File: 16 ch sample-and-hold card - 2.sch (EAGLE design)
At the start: 80 parts, among them IC1 TL074D, IC3 TL074D, IC4 TL074D, IC7 TL074D, IC9 MAX306CWI

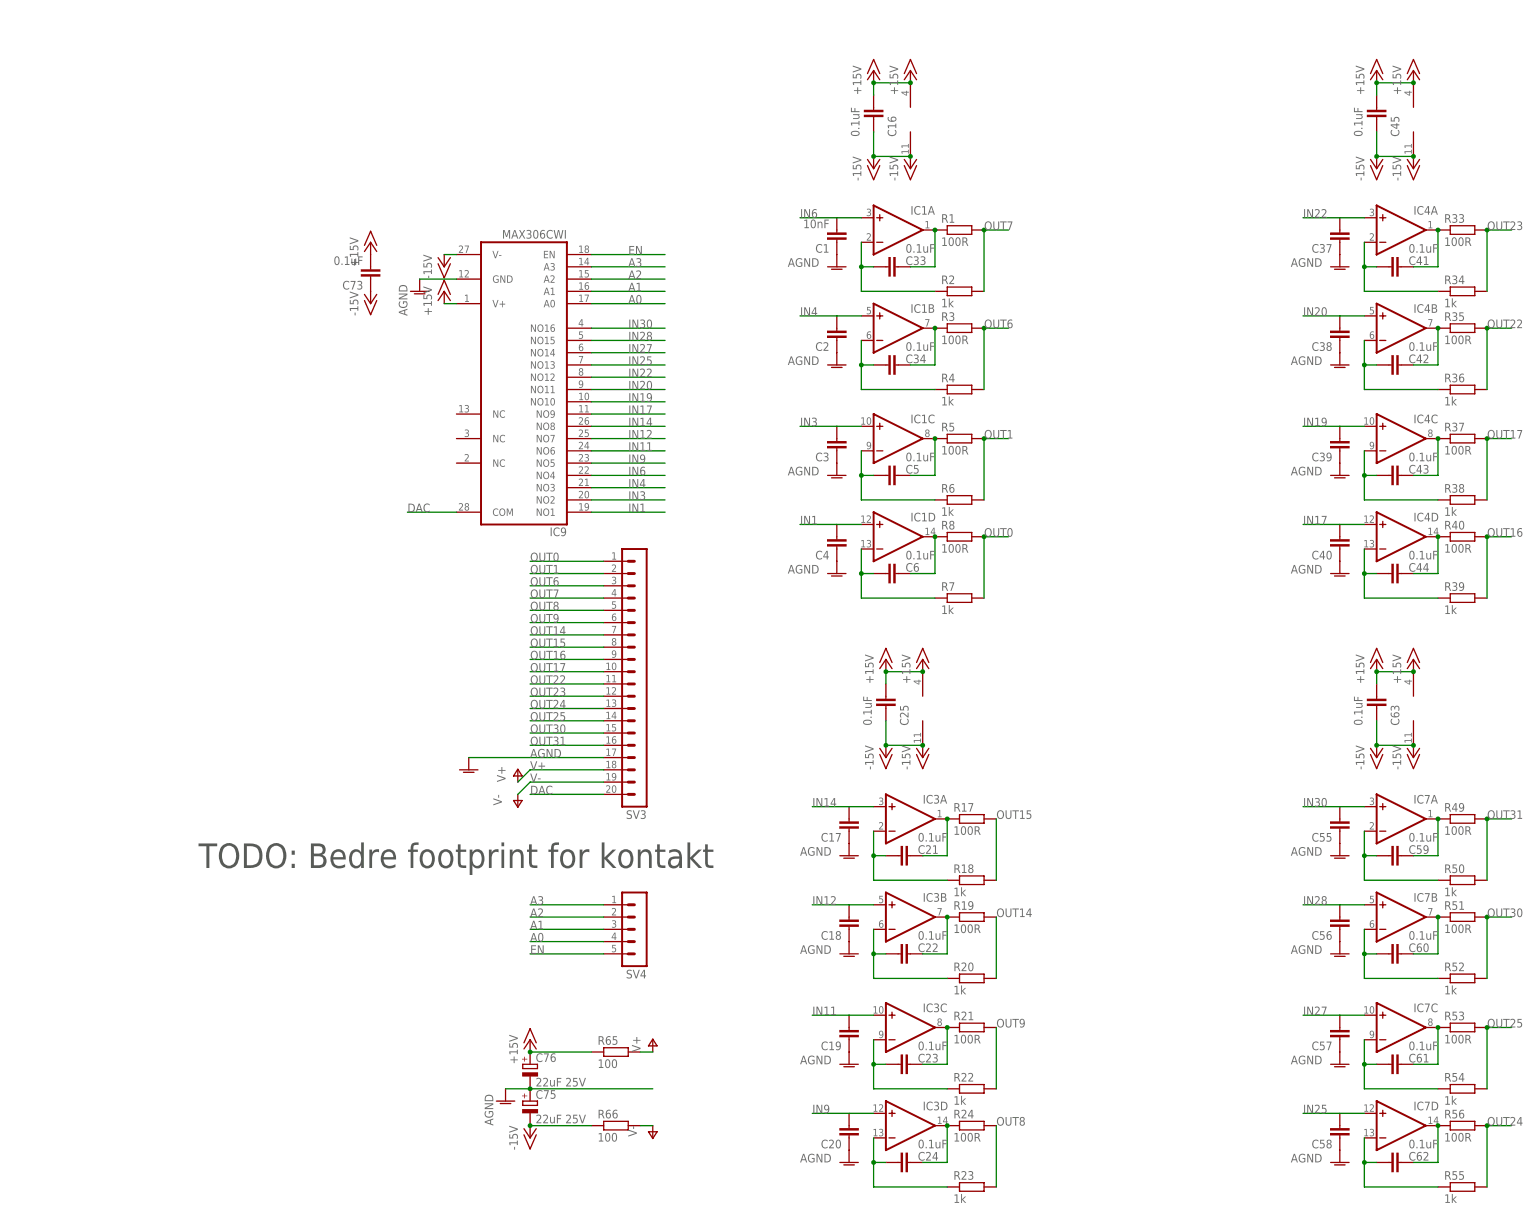
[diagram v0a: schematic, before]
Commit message: Reworked resistor and electrolytic caps placement to tap power AFTER caps for better noise filtering
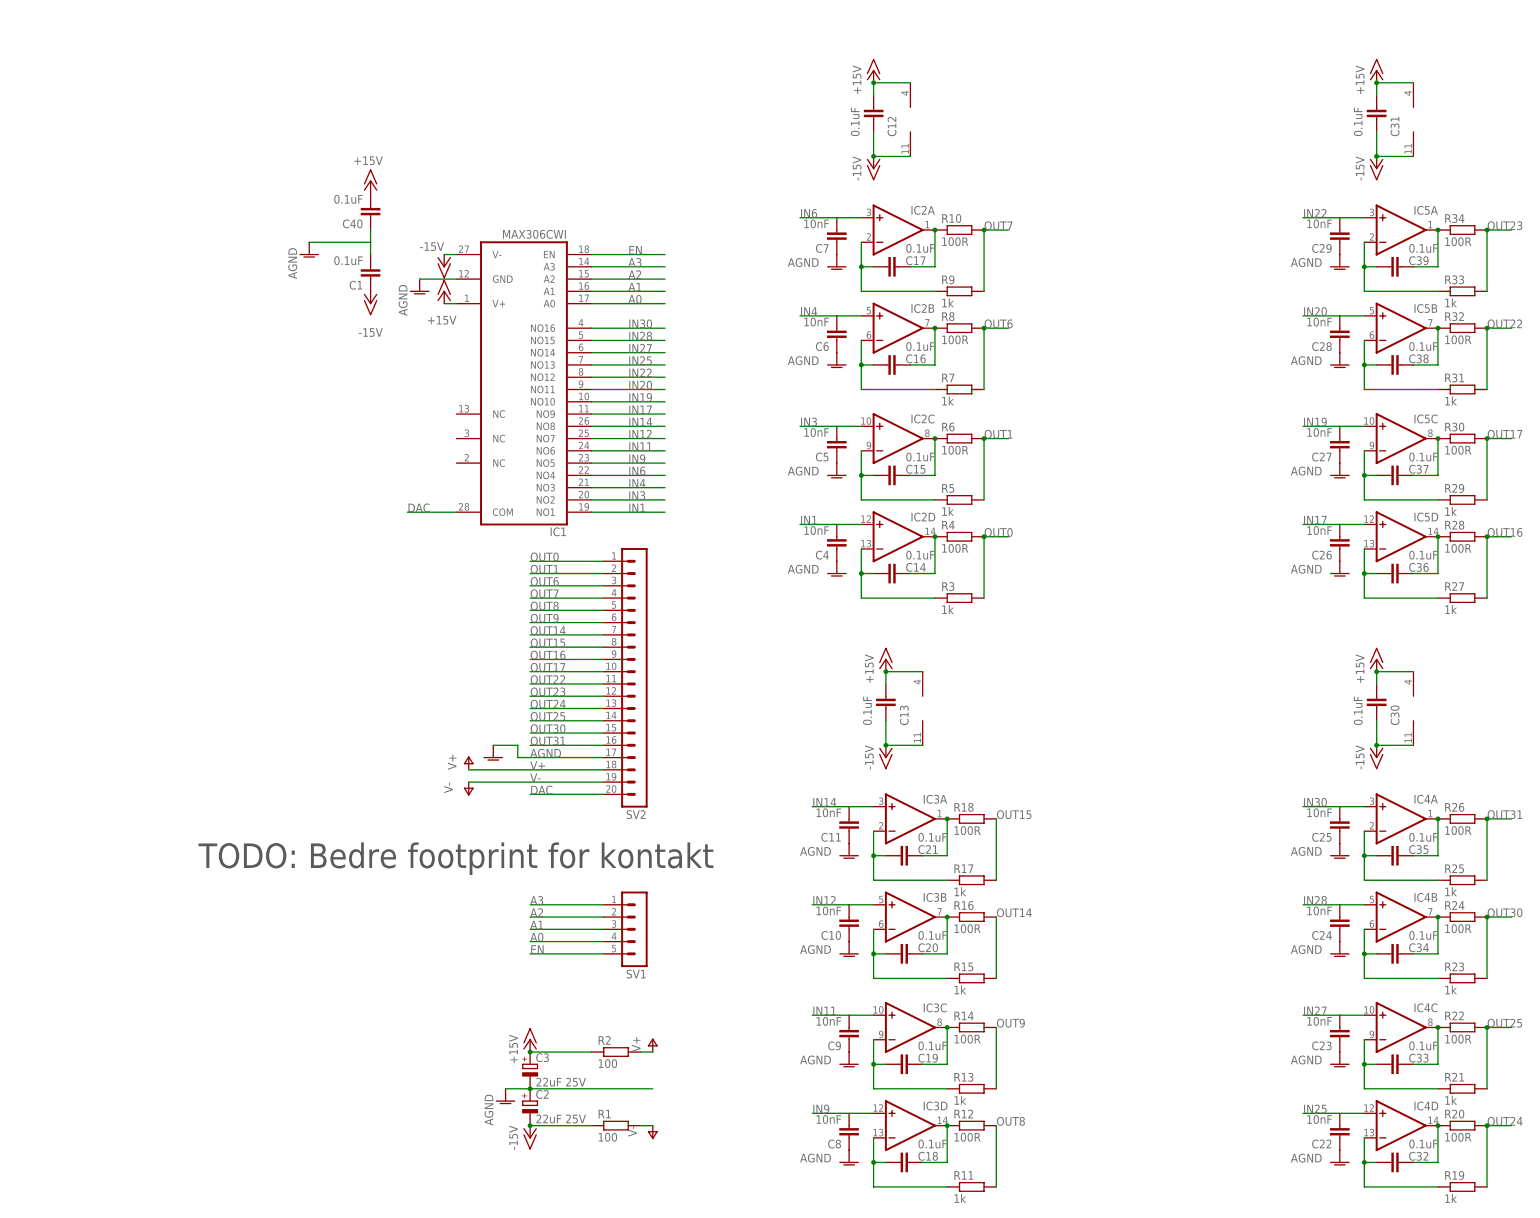
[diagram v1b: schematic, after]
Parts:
- removed C41, C42, C43, C60, C61, C73: 0.1uF, resistor:C-EUC0603
- removed C55, C56, C57, C58: (no value), resistor:C-EUC1206
- removed C75, C76: 22uF 25V, resistor:CPOL-EUE2-5
- removed IC7: TL074D, linear:TL074D
- removed IC9: MAX306CWI, maxim:MAX306CWI
- removed R51, R53, R56: 100R, resistor:R-EU_R0603
- removed R52, R54, R55: 1k, resistor:R-EU_R0603
- removed R65, R66: 100, resistor:R-EU_0207/7
- added C10, C11, C26, C27, C28, C29, C7, C8, C9: 10nF, resistor:C-EUC1206
- added C12, C13, C14, C15: 0.1uF, resistor:C-EUC0603
- added IC2, IC5: TL074D, linear:TL074D
- added R10, R12, R14, R16: 100R, resistor:R-EU_R0603
- added R11, R13, R15, R9: 1k, resistor:R-EU_R0603
- C1: value 10nF -> 0.1uF; device resistor:C-EUC1206 -> resistor:C-EUC0603
- C17, C18, C19, C20, C37, C38, C39, C40: value (none) -> 0.1uF; device resistor:C-EUC1206 -> resistor:C-EUC0603
- C2, C3: value (none) -> 22uF 25V; device resistor:C-EUC1206 -> resistor:CPOL-EUE2-5
- C22, C23, C24, C25, C5, C6: value 0.1uF -> 10nF; device resistor:C-EUC0603 -> resistor:C-EUC1206
- C4: value (none) -> 10nF
- IC1: value TL074D -> MAX306CWI; device linear:TL074D -> maxim:MAX306CWI
- R1: value 100R -> 100; device resistor:R-EU_R0603 -> resistor:R-EU_0207/7
- R17, R19, R21, R3, R33, R5: value 100R -> 1k
- R18, R20, R22, R34, R4, R6: value 1k -> 100R
- R2: value 1k -> 100; device resistor:R-EU_R0603 -> resistor:R-EU_0207/7
- renumbered C44 to C36, C45 to C31, C59 to C35, C62 to C32, C63 to C30, R35 to R32, R36 to R31, R37 to R30, R38 to R29, R39 to R27, R40 to R28, R49 to R26, R50 to R25, SV3 to SV2, SV4 to SV1
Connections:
- net +15V: now also C12.1, C13.1, C3.+, C40.2, IC1.V+, IC2P.V+, IC5P.V+, R2.1; no longer C16.1, C25.1, C73.2, C76.+, IC1P.V+, IC7P.V+, IC9.V+, R65.1
- net -15V: now also C1.1, C12.2, C13.2, C2.-, IC1.V-, IC2P.V-, IC5P.V-, R1.1; no longer C16.2, C25.2, C73.1, C75.-, IC1P.V-, IC7P.V-, IC9.V-, R66.1
- net A0: now also IC1.A0; no longer IC9.A0
- net A1: now also IC1.A1; no longer IC9.A1
- net A2: now also IC1.A2; no longer IC9.A2
- net A3: now also IC1.A3; no longer IC9.A3
- net AGND: now also C1.2, C10.1, C11.1, C2.+, C22.1, C23.1, C24.1, C25.1, C26.1, C27.1, C28.1, C29.1, C3.-, C5.1, C6.1, C7.1, C8.1, C9.1, IC1.GND; no longer C1.1, C17.1, C18.1, C19.1, C2.1, C20.1, C3.1, C37.1, C38.1, C39.1, C55.1, C56.1, C57.1, C58.1, C75.+, C76.-, IC9.GND
- net DAC: now also IC1.COM; no longer IC9.COM
- net EN: now also IC1.EN; no longer IC9.EN
- net IN1: now also IC1.NO1, IC2D.+IN; no longer IC1D.+IN, IC9.NO1
- net IN11: now also C9.2, IC1.NO6; no longer C19.2, IC9.NO6
- net IN12: now also C10.2, IC1.NO7; no longer C18.2, IC9.NO7
- net IN14: now also C11.2, IC1.NO8; no longer C17.2, IC9.NO8
- net IN17: now also C26.2, IC1.NO9, IC5D.+IN; no longer C40.2, IC4D.+IN, IC9.NO9
- net IN19: now also C27.2, IC1.NO10, IC5C.+IN; no longer C39.2, IC4C.+IN, IC9.NO10
- net IN20: now also C28.2, IC1.NO11, IC5B.+IN; no longer C38.2, IC4B.+IN, IC9.NO11
- net IN22: now also C29.2, IC1.NO12, IC5A.+IN; no longer C37.2, IC4A.+IN, IC9.NO12
- net IN25: now also C22.2, IC1.NO13, IC4D.+IN; no longer C58.2, IC7D.+IN, IC9.NO13
- net IN27: now also C23.2, IC1.NO14, IC4C.+IN; no longer C57.2, IC7C.+IN, IC9.NO14
- net IN28: now also C24.2, IC1.NO15, IC4B.+IN; no longer C56.2, IC7B.+IN, IC9.NO15
- net IN3: now also C5.2, IC1.NO2, IC2C.+IN; no longer C3.2, IC1C.+IN, IC9.NO2
- net IN30: now also C25.2, IC1.NO16, IC4A.+IN; no longer C55.2, IC7A.+IN, IC9.NO16
- net IN4: now also C6.2, IC1.NO3, IC2B.+IN; no longer C2.2, IC1B.+IN, IC9.NO3
- net IN6: now also C7.2, IC1.NO4, IC2A.+IN; no longer C1.2, IC1A.+IN, IC9.NO4
- net IN9: now also C8.2, IC1.NO5; no longer C20.2, IC9.NO5
- net N$1: now also C17.2, IC2A.-IN, R9.1; no longer C33.2, IC1A.-IN, R2.1
- net N$10: now also R17.1; no longer R18.1
- net N$19: now also C20.1, R16.1; no longer C22.1, R19.1
- net N$2: now also C17.1, IC2A.OUT, R10.1; no longer C33.1, IC1A.OUT, R1.1
- net N$20: now also C20.2, R15.1; no longer C22.2, R20.1
- net N$21: now also C19.1, R14.1; no longer C23.1, R21.1
- net N$22: now also C18.1, R12.1; no longer C24.1, R24.1
- net N$23: now also C19.2, R13.1; no longer C23.2, R22.1
- net N$24: now also C18.2, R11.1; no longer C24.2, R23.1
- net N$3: now also C16.1, IC2B.OUT, R8.1; no longer C34.1, IC1B.OUT, R3.1
- net N$33: now also C39.1, IC5A.OUT, R34.1; no longer C41.1, IC4A.OUT, R33.1
- net N$34: now also C39.2, IC5A.-IN, R33.1; no longer C41.2, IC4A.-IN, R34.1
- net N$35: now also C38.1, IC5B.OUT; no longer C42.1, IC4B.OUT
- net N$36: now also C38.2, IC5B.-IN; no longer C42.2, IC4B.-IN
- net N$37: now also C37.1, IC5C.OUT; no longer C43.1, IC4C.OUT
- net N$38: now also IC5D.OUT; no longer IC4D.OUT
- net N$39: now also C37.2, IC5C.-IN; no longer C43.2, IC4C.-IN
- net N$4: now also C15.1, IC2C.OUT, R6.1; no longer C5.1, IC1C.OUT, R5.1
- net N$40: now also IC5D.-IN; no longer IC4D.-IN
- net N$49: now also IC4A.OUT; no longer IC7A.OUT
- net N$5: now also C16.2, IC2B.-IN, R7.1; no longer C34.2, IC1B.-IN, R4.1
- net N$50: now also IC4A.-IN; no longer IC7A.-IN
- net N$51: now also C34.1, IC4B.OUT, R24.1; no longer C60.1, IC7B.OUT, R51.1
- net N$52: now also C34.2, IC4B.-IN, R23.1; no longer C60.2, IC7B.-IN, R52.1
- net N$53: now also C33.1, IC4C.OUT, R22.1; no longer C61.1, IC7C.OUT, R53.1
- net N$54: now also IC4D.OUT, R20.1; no longer IC7D.OUT, R56.1
- net N$55: now also C33.2, IC4C.-IN, R21.1; no longer C61.2, IC7C.-IN, R54.1
- net N$56: now also IC4D.-IN, R19.1; no longer IC7D.-IN, R55.1
- net N$6: now also C14.1, IC2D.OUT, R4.1; no longer C6.1, IC1D.OUT, R8.1
- net N$7: now also C15.2, IC2C.-IN, R5.1; no longer C5.2, IC1C.-IN, R6.1
- net N$8: now also C14.2, IC2D.-IN, R3.1; no longer C6.2, IC1D.-IN, R7.1
- net N$9: now also R18.1; no longer R17.1
- net OUT0: now also R3.2, R4.2; no longer R7.2, R8.2
- net OUT14: now also R15.2, R16.2; no longer R19.2, R20.2
- net OUT24: now also R19.2, R20.2; no longer R55.2, R56.2
- net OUT25: now also R21.2, R22.2; no longer R53.2, R54.2
- net OUT30: now also R23.2, R24.2; no longer R51.2, R52.2
- net OUT6: now also R7.2, R8.2; no longer R3.2, R4.2
- net OUT7: now also R10.2, R9.2; no longer R1.2, R2.2
- net OUT8: now also R11.2, R12.2; no longer R23.2, R24.2
- net OUT9: now also R13.2, R14.2; no longer R21.2, R22.2
- net V+: now also R2.2; no longer R65.2
- net V-: now also R1.2; no longer R66.2
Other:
- moved on the sheet: C1, C16, C17, C18, C19, C20, C22, C23, C24, C25, C33, C34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

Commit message: Last commit before moving multiplexer to separate repo
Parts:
- added C41, C42, C43, C44: 0.1uF, resistor:C-EUC0603
- R1, R2: value 100 -> 100R
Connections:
- net -15V: now also C41.2, C42.2, C43.2, C44.2; no longer C12.2, C13.2, C30.2, C31.2
- net AGND: now also C12.2, C13.2, C30.2, C31.2, C41.1, C42.1, C43.1, C44.1
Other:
- moved on the sheet: C12, C13, C30, C31
